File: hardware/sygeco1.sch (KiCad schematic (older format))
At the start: 12 parts, among them J1 SSD1306_module, SW1 SW_Push_DPDT, SW2 SW_Push_DPDT, U1 ATtiny85-20PU

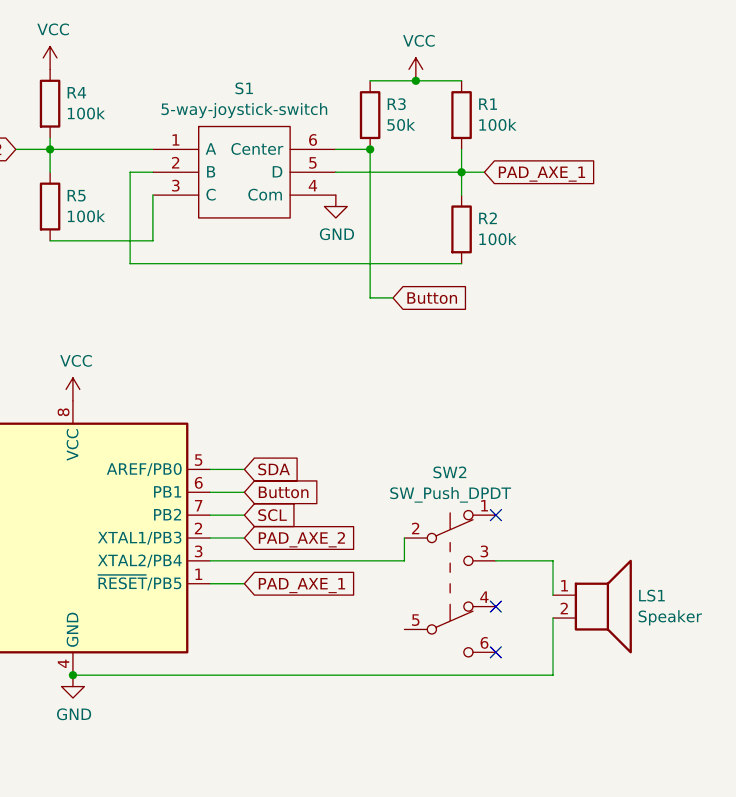
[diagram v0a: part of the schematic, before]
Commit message: add some text/logo
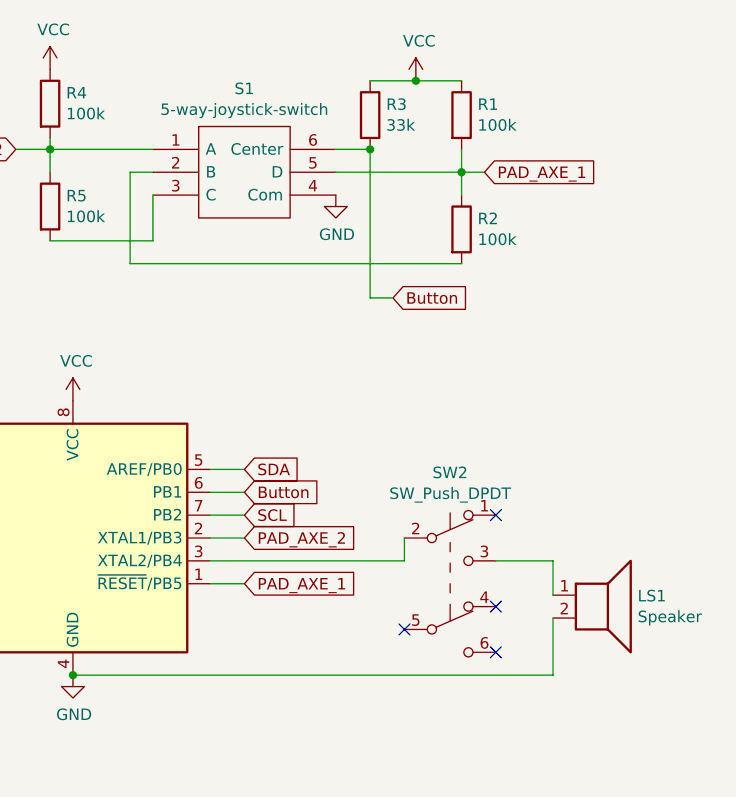
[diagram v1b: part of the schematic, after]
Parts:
- R3: value 50k -> 33k
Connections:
- no-connect marks 6 -> 7
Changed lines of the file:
@@
 P 5500 1200
 F 0 "R3" H 5570 1246 50  0000 L CNN
-F 1 "50k" H 5570 1155 50  0000 L CNN
+F 1 "33k" H 5570 1155 50  0000 L CNN
 F 2 "Resistor_SMD:R_1206_3216Metric" V 5430 1200 50  0001 C CNN
 F 3 "~" H 5500 1200 50  0001 C CNN
@@
 	-1   0    0    -1
 $EndComp
+NoConn ~ 5650 3450
 $EndSCHEMATC

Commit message: keep on 'improving'. Changed beeper and cell battery holder, according to what i can get my hand on.
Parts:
- BT1: footprint Battery:BatteryHolder_Keystone_3009_1x2450 -> sygeco:BatteryHolder_China_1x20mm
- LS1: footprint Buzzer_Beeper:Buzzer_15x7.5RM7.6 -> Buzzer_Beeper:MagneticBuzzer_ProSignal_ABT-410-RC
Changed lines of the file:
@@
 F 0 "LS1" H 6670 3296 50  0000 L CNN
 F 1 "Speaker" H 6670 3205 50  0000 L CNN
-F 2 "Buzzer_Beeper:Buzzer_15x7.5RM7.6" H 6500 3100 50  0001 C CNN
+F 2 "Buzzer_Beeper:MagneticBuzzer_ProSignal_ABT-410-RC" H 6500 3100 50  0001 C CNN
 F 3 "~" H 6490 3250 50  0001 C CNN
 	1    6500 3300
@@
 F 0 "BT1" H 1468 4246 50  0000 L CNN
 F 1 "Battery_Cell" H 1468 4155 50  0000 L CNN
-F 2 "Battery:BatteryHolder_Keystone_3009_1x2450" V 1350 4210 50  0001 C CNN
+F 2 "sygeco:BatteryHolder_China_1x20mm" V 1350 4210 50  0001 C CNN
 F 3 "~" V 1350 4210 50  0001 C CNN
 	1    1350 4150

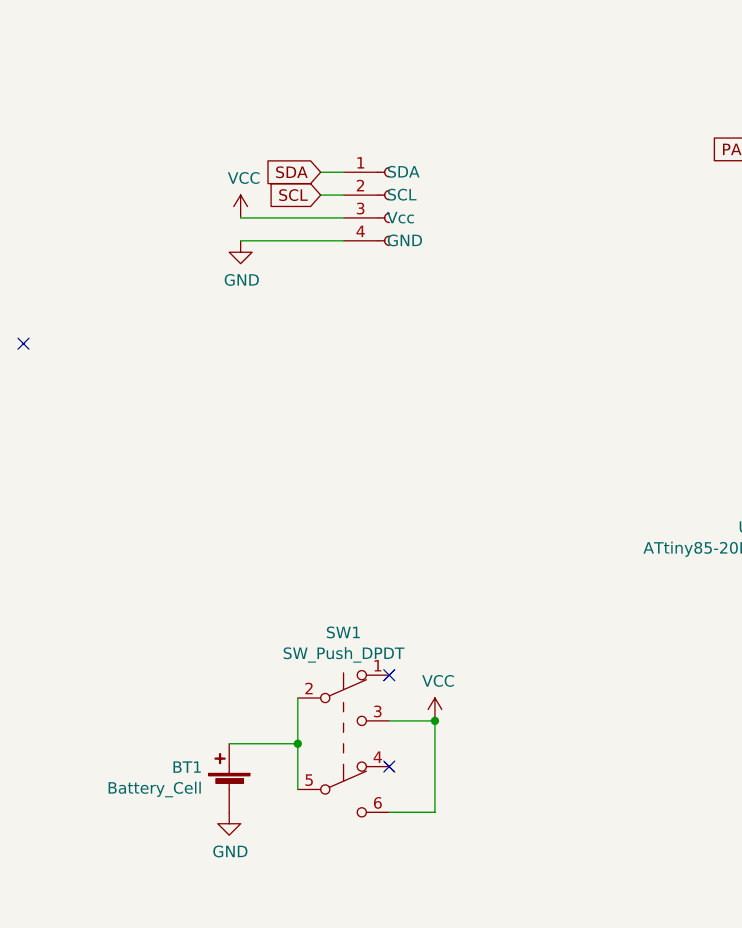
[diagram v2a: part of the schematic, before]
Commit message: add an ISP header, a power led, and redo completely the routing: * the board is bigger, but hopefully more 'practical' to use * using two layers of copper. it's the same price, why bother ?
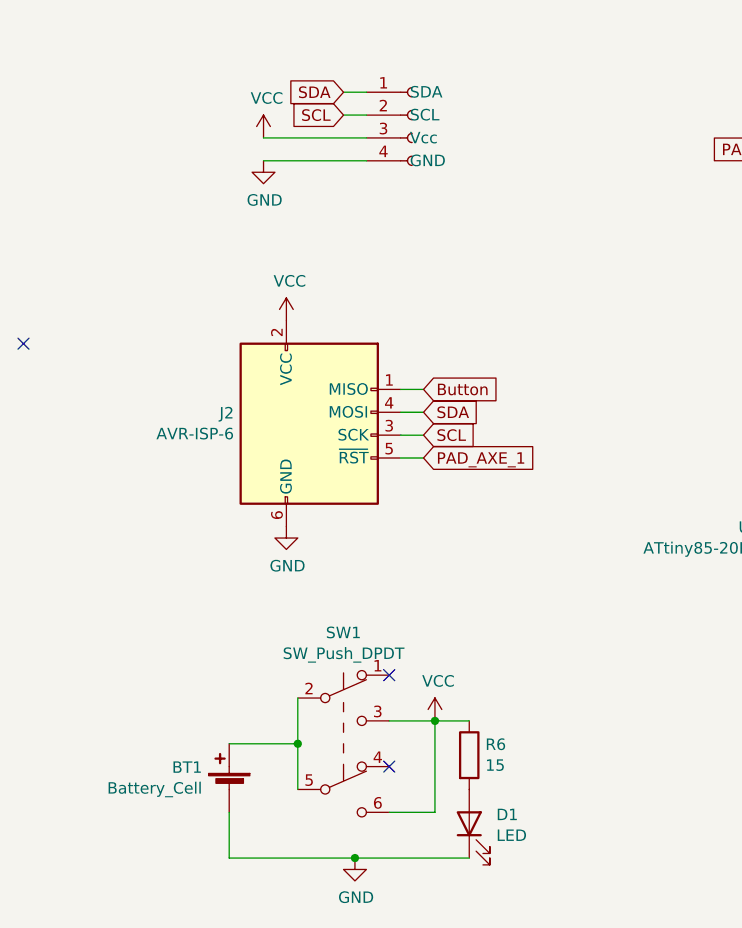
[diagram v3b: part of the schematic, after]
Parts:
- added D1: LED, LED_SMD:LED_1206_3216Metric, symbol Device:LED
- added J2: AVR-ISP-6, Connector_PinHeader_2.54mm:PinHeader_2x03_P2.54mm_Vertical, symbol Connector:AVR-ISP-6
- added R6: 15, Resistor_SMD:R_1206_3216Metric, symbol Device:R
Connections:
- net Button: now also J2.1 (MISO)
- net GND: now also D1.1 (K), J2.6 (GND)
- net PAD_AXE_1: now also J2.5 (~RST)
- net SCL: now also J2.3 (SCK)
- net SDA: now also J2.4 (MOSI)
- net VCC: now also J2.2 (VCC), R6.1
- new net: D1.2 (A), R6.2
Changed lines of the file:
@@
 L power:GND #PWR0101
 U 1 1 5FA31FF1
-P 1350 4250
-F 0 "#PWR0101" H 1350 4000 50  0001 C CNN
-F 1 "GND" H 1355 4077 50  0000 C CNN
-F 2 "" H 1350 4250 50  0001 C CNN
-F 3 "" H 1350 4250 50  0001 C CNN
-	1    1350 4250
+P 1900 4450
+F 0 "#PWR0101" H 1900 4200 50  0001 C CNN
+F 1 "GND" H 1905 4277 50  0000 C CNN
+F 2 "" H 1900 4450 50  0001 C CNN
+F 3 "" H 1900 4450 50  0001 C CNN
+	1    1900 4450
 	1    0    0    -1
 $EndComp
@@
 L sygeco1_symbols:SSD1306_module J1
 U 1 1 5FA9DE86
-P 2050 1550
-F 0 "J1" H 2078 1526 50  0001 L CNN
-F 1 "SSD1306_module" H 2078 1435 50  0001 L CNN
-F 2 "Connector_PinSocket_2.54mm:PinSocket_1x04_P2.54mm_Vertical" H 2050 1550 50  0001 C CNN
-F 3 "~" H 2050 1550 50  0001 C CNN
-	1    2050 1550
-	1    0    0    -1
-$EndComp
-Text GLabel 1750 1450 0    50   Input ~ 0
+P 2150 1200
+F 0 "J1" H 2178 1176 50  0001 L CNN
+F 1 "SSD1306_module" H 2178 1085 50  0001 L CNN
+F 2 "Connector_PinSocket_2.54mm:PinSocket_1x04_P2.54mm_Vertical" H 2150 1200 50  0001 C CNN
+F 3 "~" H 2150 1200 50  0001 C CNN
+	1    2150 1200
+	1    0    0    -1
+$EndComp
+Text GLabel 1850 1100 0    50   Input ~ 0
 SDA
-Text GLabel 1750 1550 0    50   Input ~ 0
+Text GLabel 1850 1200 0    50   Input ~ 0
 SCL
 $Comp
 L power:GND #PWR0108
 U 1 1 5FAA304D
-P 1400 1750
-F 0 "#PWR0108" H 1400 1500 50  0001 C CNN
-F 1 "GND" H 1405 1577 50  0000 C CNN
-F 2 "" H 1400 1750 50  0001 C CNN
-F 3 "" H 1400 1750 50  0001 C CNN
-	1    1400 1750
+P 1500 1400
+F 0 "#PWR0108" H 1500 1150 50  0001 C CNN
+F 1 "GND" H 1505 1227 50  0000 C CNN
+F 2 "" H 1500 1400 50  0001 C CNN
+F 3 "" H 1500 1400 50  0001 C CNN
+	1    1500 1400
 	1    0    0    -1
 $EndComp
@@
 L power:VCC #PWR0109
 U 1 1 5FAA635F
-P 1400 1650
-F 0 "#PWR0109" H 1400 1500 50  0001 C CNN
-F 1 "VCC" H 1415 1823 50  0000 C CNN
-F 2 "" H 1400 1650 50  0001 C CNN
-F 3 "" H 1400 1650 50  0001 C CNN
-	1    1400 1650
-	1    0    0    -1
-$EndComp
-Wire Wire Line
-	1850 1650 1400 1650
-Wire Wire Line
-	1400 1750 1850 1750
-Wire Wire Line
-	1850 1550 1750 1550
-Wire Wire Line
-	1850 1450 1750 1450
+P 1500 1300
+F 0 "#PWR0109" H 1500 1150 50  0001 C CNN
+F 1 "VCC" H 1515 1473 50  0000 C CNN
+F 2 "" H 1500 1300 50  0001 C CNN
+F 3 "" H 1500 1300 50  0001 C CNN
+	1    1500 1300
+	1    0    0    -1
+$EndComp
+Wire Wire Line
+	1950 1300 1500 1300
+Wire Wire Line
+	1500 1400 1950 1400
+Wire Wire Line
+	1950 1200 1850 1200
+Wire Wire Line
+	1950 1100 1850 1100
 $Comp
 L sygeco1_symbols:5-way-joystick-switch S1
@@
 Wire Wire Line
 	2250 4250 2250 3850
-Connection ~ 2250 3850
 $Comp
 L Device:Battery_Cell BT1
@@
 $EndComp
 NoConn ~ 5650 3450
+$Comp
+L Connector:AVR-ISP-6 J2
+U 1 1 5FA6E1A1
+P 1700 2600
+F 0 "J2" H 1371 2696 50  0000 R CNN
+F 1 "AVR-ISP-6" H 1371 2605 50  0000 R CNN
+F 2 "Connector_PinHeader_2.54mm:PinHeader_2x03_P2.54mm_Vertical" V 1450 2650 50  0001 C CNN
+F 3 " ~" H 425 2050 50  0001 C CNN
+	1    1700 2600
+	1    0    0    -1
+$EndComp
+$Comp
+L power:GND #PWR04
+U 1 1 5FA6F2B8
+P 1600 3000
+F 0 "#PWR04" H 1600 2750 50  0001 C CNN
+F 1 "GND" H 1605 2827 50  0000 C CNN
+F 2 "" H 1600 3000 50  0001 C CNN
+F 3 "" H 1600 3000 50  0001 C CNN
+	1    1600 3000
+	1    0    0    -1
+$EndComp
+$Comp
+L power:VCC #PWR03
+U 1 1 5FA6FB2B
+P 1600 2100
+F 0 "#PWR03" H 1600 1950 50  0001 C CNN
+F 1 "VCC" H 1615 2273 50  0000 C CNN
+F 2 "" H 1600 2100 50  0001 C CNN
+F 3 "" H 1600 2100 50  0001 C CNN
+	1    1600 2100
+	1    0    0    -1
+$EndComp
+Text GLabel 2200 2700 2    50   Input ~ 0
+PAD_AXE_1
+Text GLabel 2200 2600 2    50   Input ~ 0
+SCL
+Text GLabel 2200 2500 2    50   Input ~ 0
+SDA
+Text GLabel 2200 2400 2    50   Input ~ 0
+Button
+Wire Wire Line
+	2100 2400 2200 2400
+Wire Wire Line
+	2100 2500 2200 2500
+Wire Wire Line
+	2100 2600 2200 2600
+Wire Wire Line
+	2100 2700 2200 2700
+$Comp
+L Device:R R6
+U 1 1 5FA79D6B
+P 2400 4000
+F 0 "R6" H 2470 4046 50  0000 L CNN
+F 1 "15" H 2470 3955 50  0000 L CNN
+F 2 "Resistor_SMD:R_1206_3216Metric" V 2330 4000 50  0001 C CNN
+F 3 "~" H 2400 4000 50  0001 C CNN
+	1    2400 4000
+	1    0    0    -1
+$EndComp
+$Comp
+L Device:LED D1
+U 1 1 5FA7AC0D
+P 2400 4300
+F 0 "D1" V 2439 4182 50  0000 R CNN
+F 1 "LED" V 2348 4182 50  0000 R CNN
+F 2 "LED_SMD:LED_1206_3216Metric" H 2400 4300 50  0001 C CNN
+F 3 "~" H 2400 4300 50  0001 C CNN
+	1    2400 4300
+	0    -1   -1   0
+$EndComp
+Connection ~ 2250 3850
+Wire Wire Line
+	2400 4450 1900 4450
+Wire Wire Line
+	1900 4450 1350 4450
+Wire Wire Line
+	1350 4450 1350 4250
+Connection ~ 1900 4450
+Wire Wire Line
+	2400 3850 2250 3850
 $EndSCHEMATC

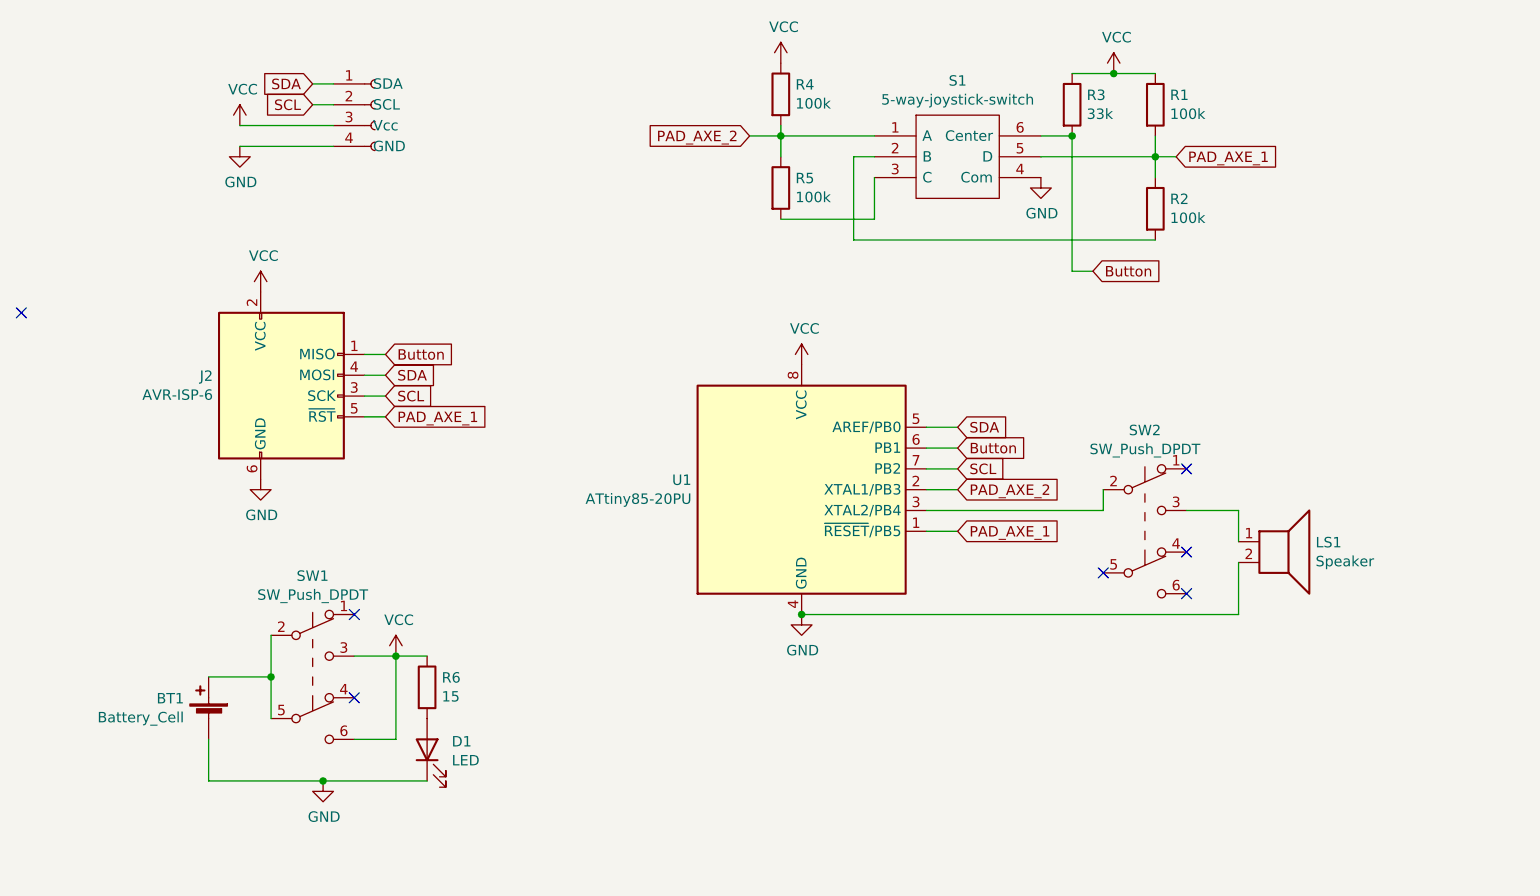
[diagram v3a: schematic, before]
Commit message: add decoupling capacitor, use same value for keypad resistors, it's simpler
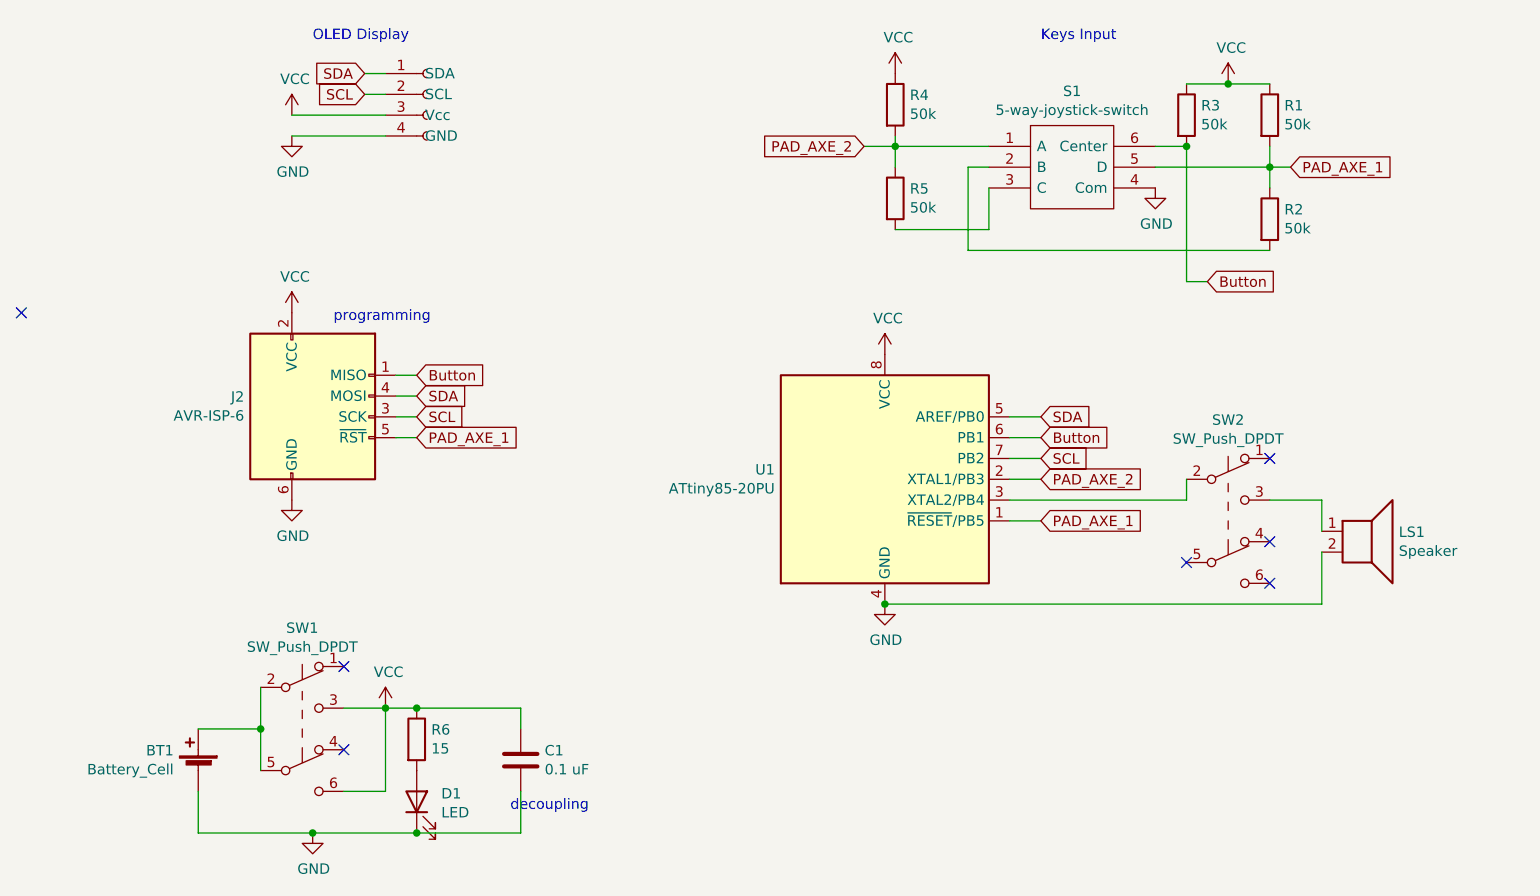
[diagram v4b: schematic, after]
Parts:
- added C1: 0.1 uF, Capacitor_SMD:C_1206_3216Metric_Pad1.33x1.80mm_HandSolder, symbol Device:C
- R1, R2, R4, R5: value 100k -> 50k; footprint Resistor_SMD:R_1206_3216Metric -> Resistor_SMD:R_1206_3216Metric_Pad1.30x1.75mm_HandSolder
- R3: value 33k -> 50k; footprint Resistor_SMD:R_1206_3216Metric -> Resistor_SMD:R_1206_3216Metric_Pad1.30x1.75mm_HandSolder
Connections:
- net GND: now also C1.2
- net VCC: now also C1.1
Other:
- note added: "Keys Input"
- note added: "OLED Display"
- note added: "decoupling"
- note added: "programming"
- moved on the sheet: BT1, D1, J2, LS1, R1, R2, R3, R4, R5, R6, S1, SW1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

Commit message: cleaning / small improvements
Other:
- note added: "ISP (programming)"
- note removed: "programming"
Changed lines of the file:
@@
 Text Notes 2800 4600 0    50   ~ 0
 decoupling
-Text Notes 1950 2250 0    50   ~ 0
-programming
+Text Notes 1900 2200 0    50   ~ 0
+ISP (programming)
 Text Notes 1850 900  0    50   ~ 0
 OLED Display
